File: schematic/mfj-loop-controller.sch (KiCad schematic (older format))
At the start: 29 parts, among them J1 Screw_Terminal_01x02, J2 Barrel_Jack, J3 Screw_Terminal_01x03, J4 Conn_01x10_Female, U1 TMR9-1212, U2 R-785.0-1.0, U3 LCC120, U4 LCC120, U5 LCC120, U6 LCC120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

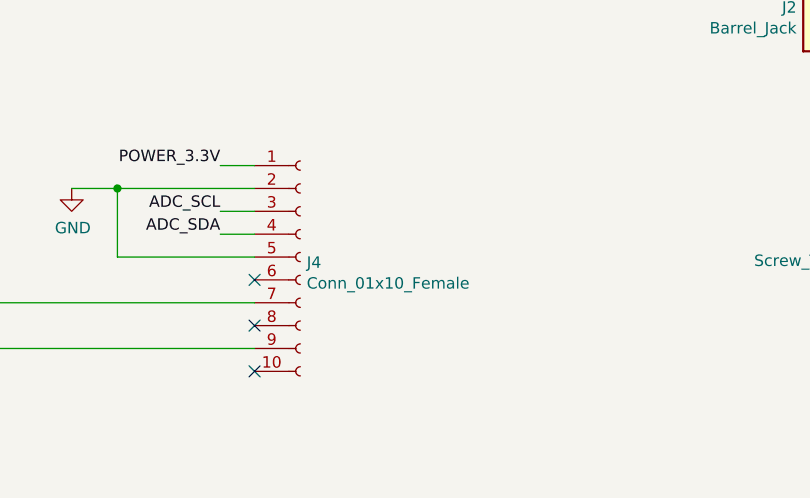
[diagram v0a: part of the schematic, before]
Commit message: Update PCB markings and version info.
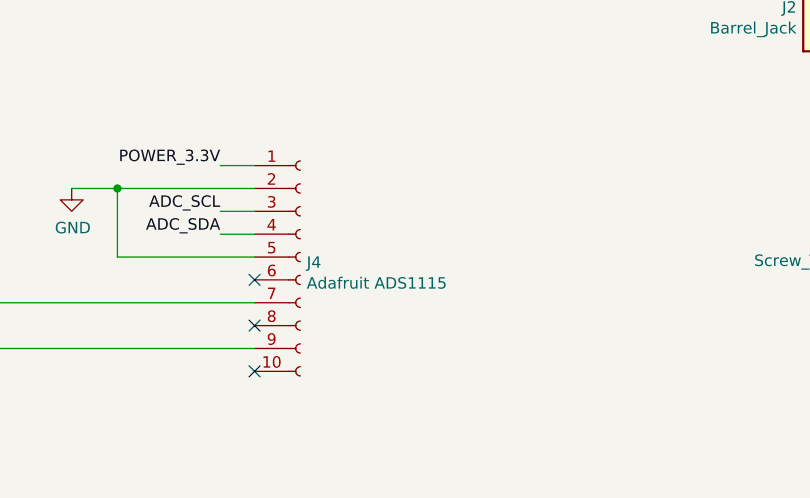
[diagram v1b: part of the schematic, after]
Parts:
- J4: value Conn_01x10_Female -> Adafruit ADS1115
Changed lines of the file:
@@
 encoding utf-8
 Sheet 1 1
-Title ""
+Title "MFJ Wi-Fi Loop Controller"
 Date ""
-Rev ""
+Rev "1.0.1"
 Comp ""
 Comment1 ""
@@
 P 4400 5700
 F 0 "J4" H 4428 5676 50  0000 L CNN
-F 1 "Conn_01x10_Female" H 4428 5585 50  0000 L CNN
+F 1 "Adafruit ADS1115" H 4428 5585 50  0000 L CNN
 F 2 "Connector_PinHeader_2.54mm:PinHeader_1x10_P2.54mm_Vertical" H 4400 5700 50  0001 C CNN
 F 3 "~" H 4400 5700 50  0001 C CNN

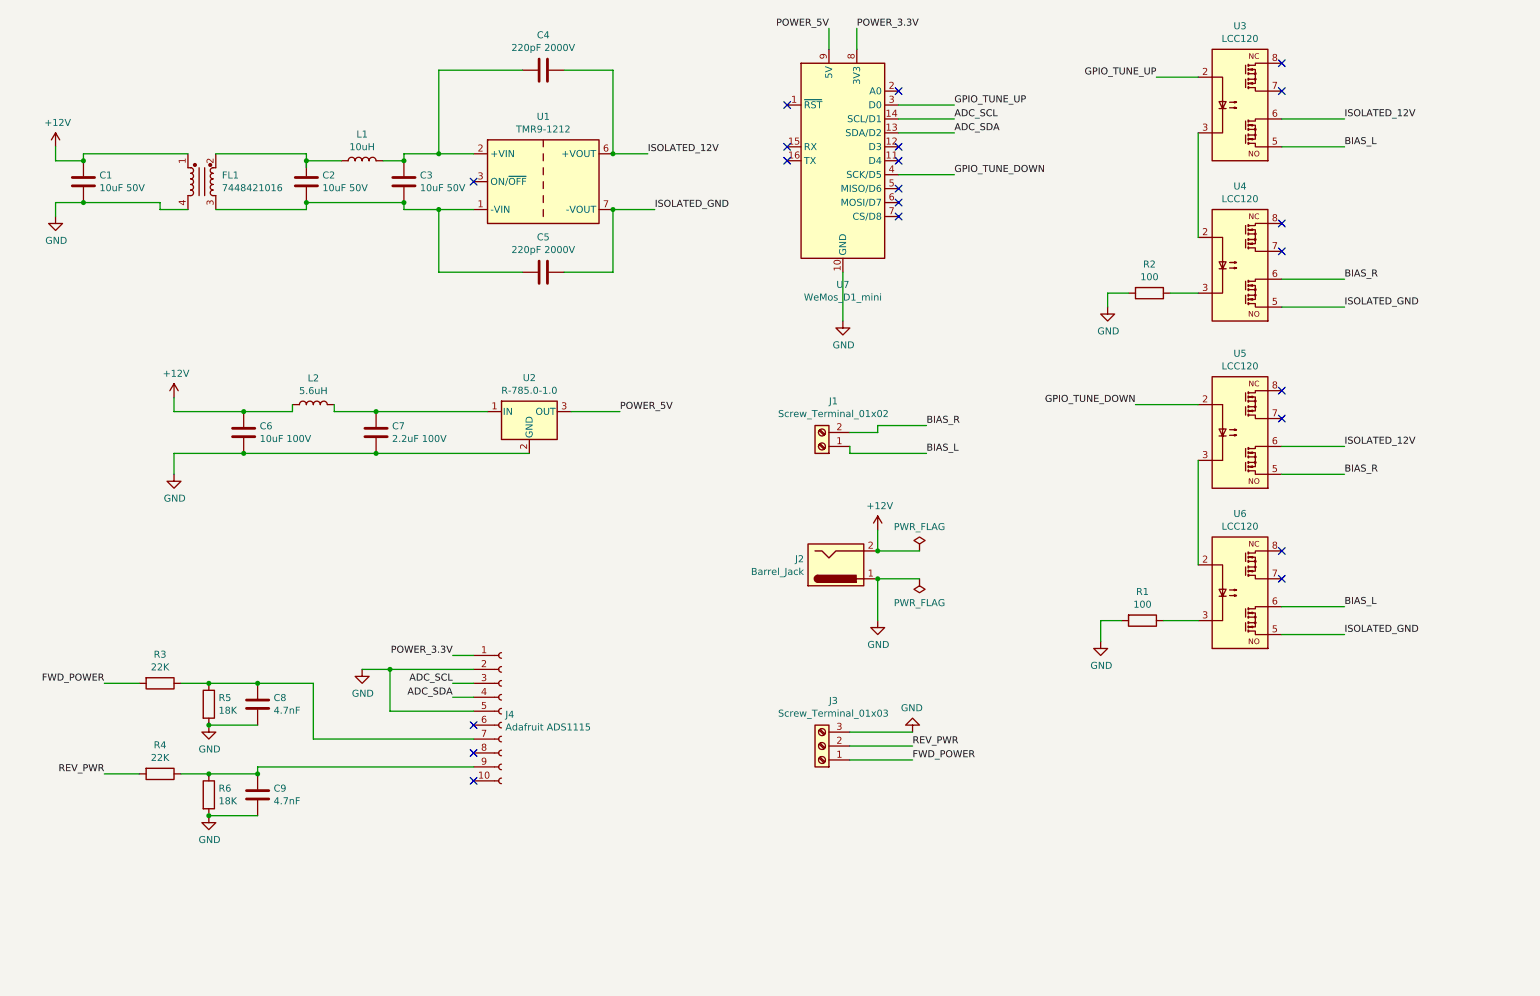
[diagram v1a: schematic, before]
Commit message: Update schematic and PCB to v1.1.0:
1. Shrink board footprint to ~4x3" for ease of mounting/EMI compliance.
2. Add mounting holes to corners.
3. Add GND/+12V flood fill layers for EMI compliance/routing.
4. Increase size of R/C/L component footprints for ease of assembly.
5. Add route for ADC alert pin to ESP82xx board.
6. Add routes for ADC analog negative pins to ground.
7. Add buffer op-amp + supporting RC filters in front of ADC.
8. Add Open Hardware logo to silkscreen.
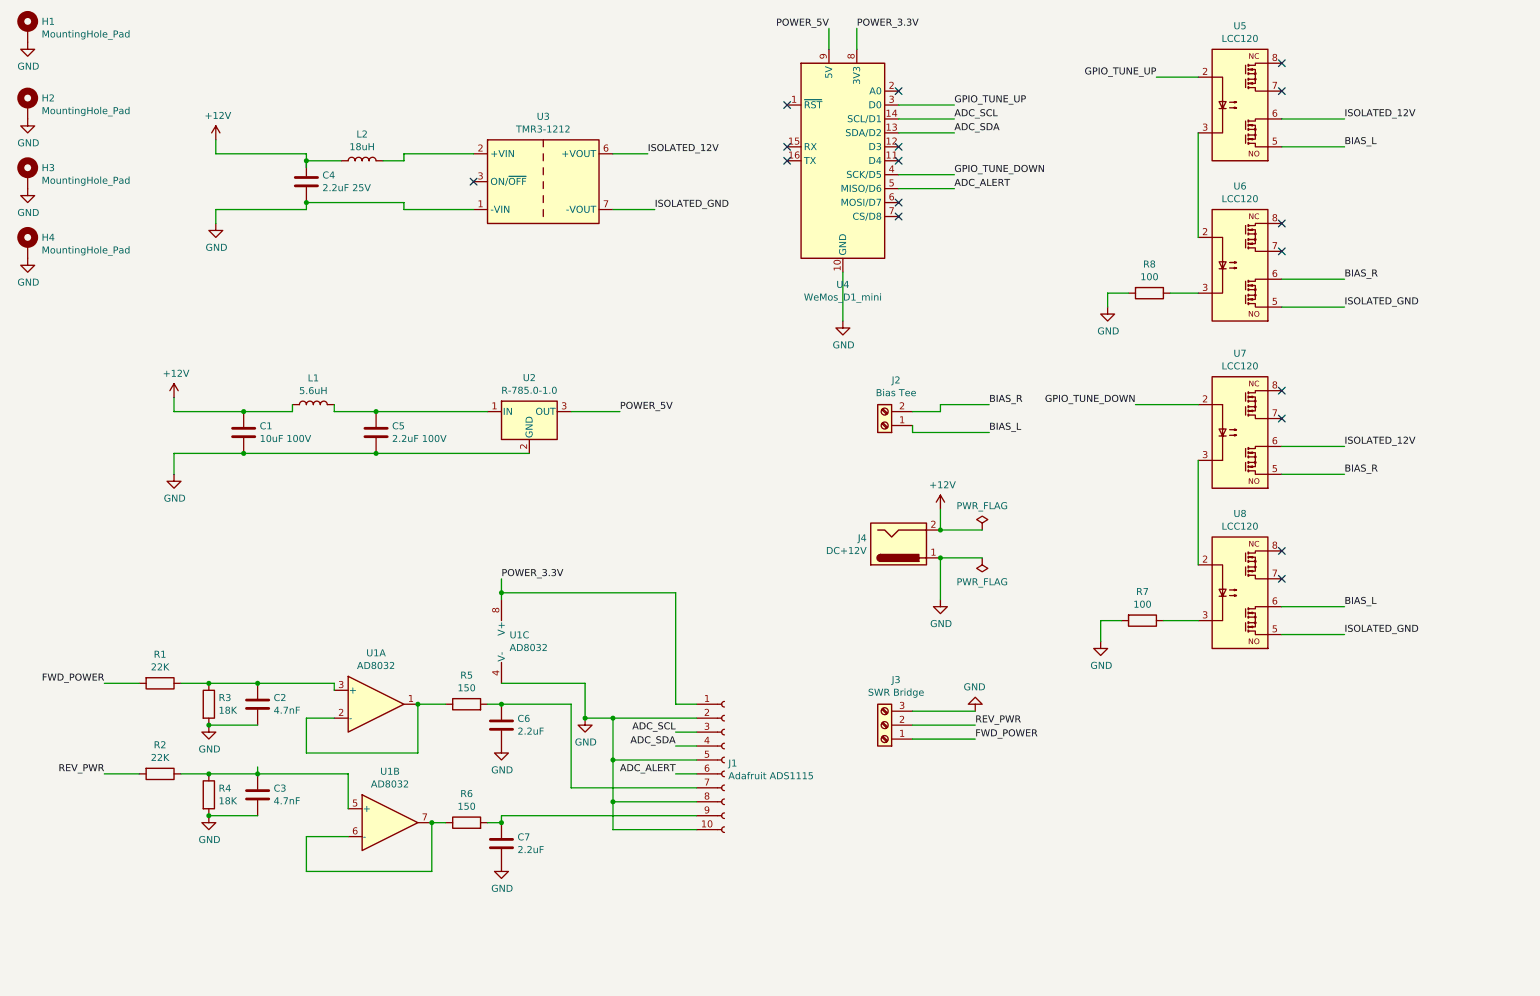
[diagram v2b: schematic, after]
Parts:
- removed C1, C3: 10uF 50V, Capacitor_THT:C_Disc_D5.0mm_W2.5mm_P2.50mm, symbol Device:C
- removed C4, C5: 220pF 2000V, Capacitor_THT:C_Disc_D10.5mm_W5.0mm_P5.00mm, symbol Device:C
- removed FL1: 7448421016, Inductor_THT:L_CommonMode_Wuerth_WE-CMB-S, symbol Device:EMI_Filter_LL_1423
- added C6, C7: 2.2uF, Capacitor_THT:C_Axial_L5.1mm_D3.1mm_P7.50mm_Horizontal, symbol Device:C
- added H1, H2, H3, H4: MountingHole_Pad, MountingHole:MountingHole_3.2mm_M3_DIN965_Pad_TopBottom, symbol Mechanical:MountingHole_Pad
- added R5, R6: 150, Resistor_THT:R_Axial_DIN0207_L6.3mm_D2.5mm_P10.16mm_Horizontal, symbol Device:R
- added U1: AD8032, Package_DIP:DIP-8_W7.62mm_Socket, symbol Amplifier_Operational:LMC6482
- C1: renamed from C6; footprint Capacitor_THT:C_Disc_D5.0mm_W2.5mm_P2.50mm -> Capacitor_THT:C_Axial_L5.1mm_D3.1mm_P7.50mm_Horizontal
- C2: renamed from C8; footprint Capacitor_THT:C_Disc_D5.0mm_W2.5mm_P2.50mm -> Capacitor_THT:C_Axial_L5.1mm_D3.1mm_P7.50mm_Horizontal
- C3: renamed from C9; footprint Capacitor_THT:C_Disc_D5.0mm_W2.5mm_P2.50mm -> Capacitor_THT:C_Axial_L5.1mm_D3.1mm_P7.50mm_Horizontal
- C4: renamed from C2; value 10uF 50V -> 2.2uF 25V; footprint Capacitor_THT:C_Disc_D5.0mm_W2.5mm_P2.50mm -> Capacitor_THT:C_Axial_L5.1mm_D3.1mm_P7.50mm_Horizontal
- C5: renamed from C7; footprint Capacitor_THT:C_Disc_D5.0mm_W2.5mm_P2.50mm -> Capacitor_THT:C_Axial_L5.1mm_D3.1mm_P7.50mm_Horizontal
- J2: renamed from J1; value Screw_Terminal_01x02 -> Bias Tee
- J3: value Screw_Terminal_01x03 -> SWR Bridge
- J4: renamed from J2; value Barrel_Jack -> DC+12V
- L1: renamed from L2; footprint Inductor_THT:L_Axial_L7.0mm_D3.3mm_P2.54mm_Vertical_Fastron_MICC -> Inductor_THT:L_Axial_L5.3mm_D2.2mm_P10.16mm_Horizontal_Vishay_IM-1
- L2: renamed from L1; value 10uH -> 18uH; footprint Inductor_THT:L_Axial_L7.0mm_D3.3mm_P2.54mm_Vertical_Fastron_MICC -> Inductor_THT:L_Axial_L5.3mm_D2.2mm_P10.16mm_Horizontal_Vishay_IM-1
- R1: renamed from R3; footprint Resistor_THT:R_Axial_DIN0207_L6.3mm_D2.5mm_P2.54mm_Vertical -> Resistor_THT:R_Axial_DIN0207_L6.3mm_D2.5mm_P10.16mm_Horizontal
- R2: renamed from R4; footprint Resistor_THT:R_Axial_DIN0207_L6.3mm_D2.5mm_P2.54mm_Vertical -> Resistor_THT:R_Axial_DIN0207_L6.3mm_D2.5mm_P10.16mm_Horizontal
- R3: renamed from R5; footprint Resistor_THT:R_Axial_DIN0207_L6.3mm_D2.5mm_P2.54mm_Vertical -> Resistor_THT:R_Axial_DIN0207_L6.3mm_D2.5mm_P10.16mm_Horizontal
- R4: renamed from R6; footprint Resistor_THT:R_Axial_DIN0207_L6.3mm_D2.5mm_P2.54mm_Vertical -> Resistor_THT:R_Axial_DIN0207_L6.3mm_D2.5mm_P10.16mm_Horizontal
- R7: renamed from R1; footprint Resistor_THT:R_Axial_DIN0207_L6.3mm_D2.5mm_P2.54mm_Vertical -> Resistor_THT:R_Axial_DIN0207_L6.3mm_D2.5mm_P10.16mm_Horizontal
- R8: renamed from R2; footprint Resistor_THT:R_Axial_DIN0207_L6.3mm_D2.5mm_P2.54mm_Vertical -> Resistor_THT:R_Axial_DIN0207_L6.3mm_D2.5mm_P10.16mm_Horizontal
- U3: renamed from U1; value TMR9-1212 -> TMR3-1212
- U5: renamed from U3; footprint Package_DIP:DIP-8_W7.62mm -> Package_DIP:DIP-8_W7.62mm_Socket
- U6: renamed from U4; footprint Package_DIP:DIP-8_W7.62mm -> Package_DIP:DIP-8_W7.62mm_Socket
- U7: renamed from U5; footprint Package_DIP:DIP-8_W7.62mm -> Package_DIP:DIP-8_W7.62mm_Socket
- U8: renamed from U6; footprint Package_DIP:DIP-8_W7.62mm -> Package_DIP:DIP-8_W7.62mm_Socket
- renumbered J4 to J1, U7 to U4
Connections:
- net +12V: now also C4.1, L2.1
- net GND: now also C4.2, J1.10 (Pin_10), J1.8 (Pin_8), U3.1 (-VIN), C6.2, C7.2, H1.1, H2.1, H3.1, H4.1, U1.4 (V-)
- net POWER_3.3V: now also U1.8 (V+)
- net ADC_ALERT: now reaches U4.5 (MISO/D6)
- net ADC_ALERT: now also J1.6 (Pin_6)
- net at C2.1, R1.1, R3.1: now also U1.3 (+); no longer J1.7 (Pin_7)
- net at C3.1, R2.1, R4.1: now also U1.5 (+); no longer J1.9 (Pin_9)
- new net: R5.1, U1.1, U1.2 (-)
- new net: R6.1, U1.6 (-), U1.7
- new net: C6.1, J1.7 (Pin_7), R5.2
- new net: C7.1, J1.9 (Pin_9), R6.2
- no-connect marks 21 -> 17
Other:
- moved on the sheet: J1, J2, J3, J4

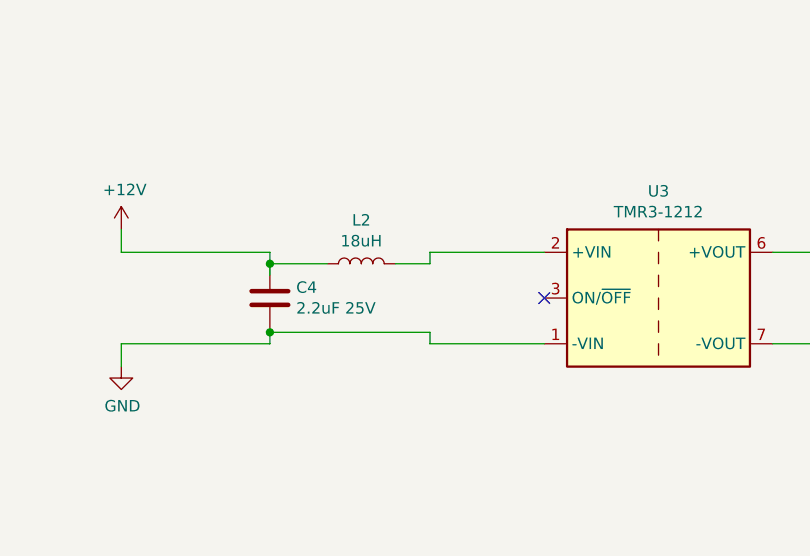
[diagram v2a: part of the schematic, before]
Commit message: Update design rules.
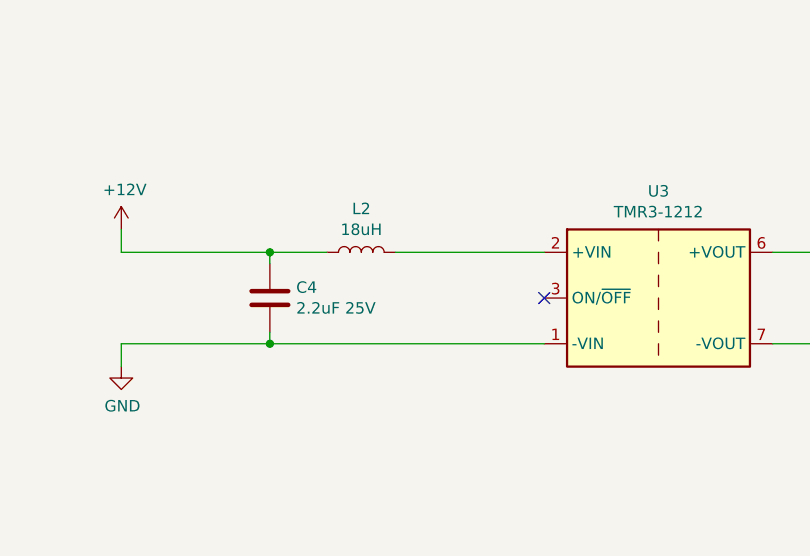
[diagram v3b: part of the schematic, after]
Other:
- moved on the sheet: L2
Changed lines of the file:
@@
 L Device:L L2
 U 1 1 5F8E8642
-P 3400 1750
-F 0 "L2" V 3590 1750 50  0000 C CNN
-F 1 "18uH" V 3499 1750 50  0000 C CNN
-F 2 "Inductor_THT:L_Axial_L5.3mm_D2.2mm_P10.16mm_Horizontal_Vishay_IM-1" H 3400 1750 50  0001 C CNN
-F 3 "~" H 3400 1750 50  0001 C CNN
-	1    3400 1750
+P 3400 1700
+F 0 "L2" V 3590 1700 50  0000 C CNN
+F 1 "18uH" V 3499 1700 50  0000 C CNN
+F 2 "Inductor_THT:L_Axial_L5.3mm_D2.2mm_P10.16mm_Horizontal_Vishay_IM-1" H 3400 1700 50  0001 C CNN
+F 3 "~" H 3400 1700 50  0001 C CNN
+	1    3400 1700
 	0    -1   -1   0
 $EndComp
-Wire Wire Line
-	3000 1800 3000 1750
-Wire Wire Line
-	3250 1750 3000 1750
-Connection ~ 3000 1750
-Wire Wire Line
-	3000 2050 3700 2050
-Wire Wire Line
-	3550 1750 3700 1750
 $Comp
 L power:GND #PWR06
@@
 Wire Wire Line
 	2350 1700 2350 1600
-Wire Wire Line
-	3700 2100 3700 2050
-Wire Wire Line
-	3700 1700 3700 1750
 NoConn ~ 4200 1900
 Text Label 5500 2100 0    50   ~ 0
@@
 Wire Wire Line
 	3000 2100 3000 2050
-Connection ~ 3000 2050
 $Comp
 L Connector:Conn_01x10_Female J1
@@
 Wire Wire Line
 	5650 6150 5800 6150
-Wire Wire Line
-	3700 1700 4200 1700
-Wire Wire Line
-	3700 2100 4200 2100
 $Comp
 L Mechanical:MountingHole_Pad H1
@@
 	1    0    0    -1
 $EndComp
+Wire Wire Line
+	4200 2100 3000 2100
+Connection ~ 3000 2100
+Wire Wire Line
+	3550 1700 4200 1700
+Wire Wire Line
+	3250 1700 3000 1700
+Connection ~ 3000 1700
 $EndSCHEMATC

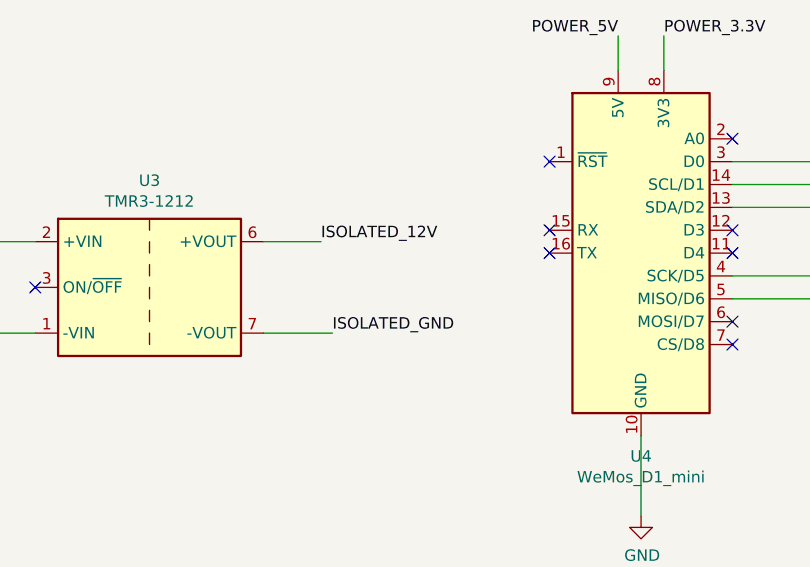
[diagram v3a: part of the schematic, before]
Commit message: Add minimum load to 12V isolated supply to reduce tuning noise.
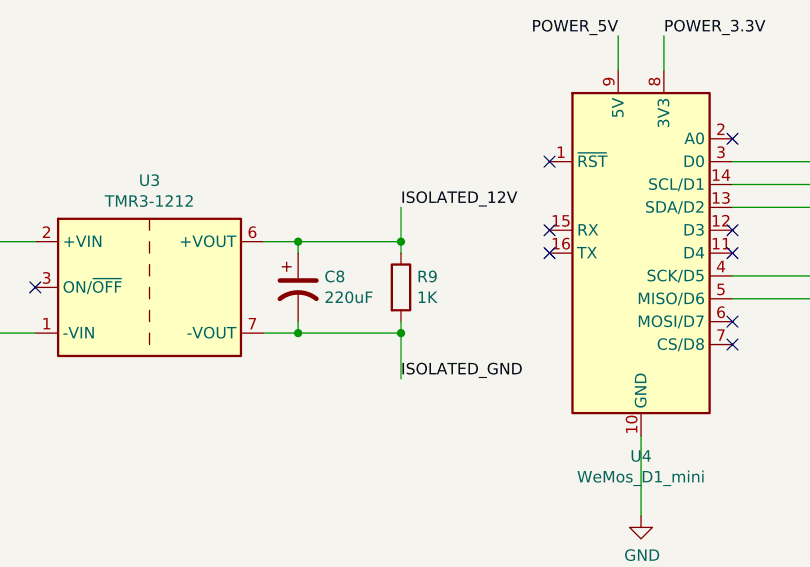
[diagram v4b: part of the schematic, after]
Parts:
- added C8: 220uF, Capacitor_THT:CP_Radial_D6.3mm_P2.50mm, symbol Device:CP1
- added R9: 1K, Resistor_THT:R_Axial_DIN0207_L6.3mm_D2.5mm_P10.16mm_Horizontal, symbol Device:R
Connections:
- net ISOLATED_12V: now also C8.1, R9.1
- net ISOLATED_GND: now also C8.2, R9.2
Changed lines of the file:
@@
 	2350 1700 2350 1600
 NoConn ~ 4200 1900
-Text Label 5500 2100 0    50   ~ 0
-ISOLATED_GND
-Text Label 5450 1700 0    50   ~ 0
-ISOLATED_12V
-Wire Wire Line
-	5450 1700 5200 1700
-Wire Wire Line
-	5500 2100 5200 2100
 $Comp
 L Device:C C1
@@
 	3250 1700 3000 1700
 Connection ~ 3000 1700
+$Comp
+L Device:CP1 C8
+U 1 1 5FB4E006
+P 5350 1900
+F 0 "C8" H 5465 1946 50  0000 L CNN
+F 1 "220uF" H 5465 1855 50  0000 L CNN
+F 2 "Capacitor_THT:CP_Radial_D6.3mm_P2.50mm" H 5350 1900 50  0001 C CNN
+F 3 "~" H 5350 1900 50  0001 C CNN
+	1    5350 1900
+	1    0    0    -1
+$EndComp
+Wire Wire Line
+	5350 1750 5350 1700
+Connection ~ 5350 1700
+Wire Wire Line
+	5350 1700 5200 1700
+Wire Wire Line
+	5350 2050 5350 2100
+Connection ~ 5350 2100
+Wire Wire Line
+	5350 2100 5200 2100
+$Comp
+L Device:R R9
+U 1 1 5FB62970
+P 5800 1900
+F 0 "R9" H 5870 1946 50  0000 L CNN
+F 1 "1K" H 5870 1855 50  0000 L CNN
+F 2 "Resistor_THT:R_Axial_DIN0207_L6.3mm_D2.5mm_P10.16mm_Horizontal" V 5730 1900 50  0001 C CNN
+F 3 "~" H 5800 1900 50  0001 C CNN
+	1    5800 1900
+	1    0    0    -1
+$EndComp
+Wire Wire Line
+	5800 1700 5800 1750
+Wire Wire Line
+	5350 1700 5800 1700
+Wire Wire Line
+	5800 2100 5800 2050
+Wire Wire Line
+	5350 2100 5800 2100
+Text Label 5800 2300 0    50   ~ 0
+ISOLATED_GND
+Text Label 5800 1550 0    50   ~ 0
+ISOLATED_12V
+Wire Wire Line
+	5800 1550 5800 1700
+Connection ~ 5800 1700
+Wire Wire Line
+	5800 2100 5800 2300
+Connection ~ 5800 2100
 $EndSCHEMATC
